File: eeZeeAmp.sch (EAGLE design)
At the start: 12 parts, among them IC1 LM386

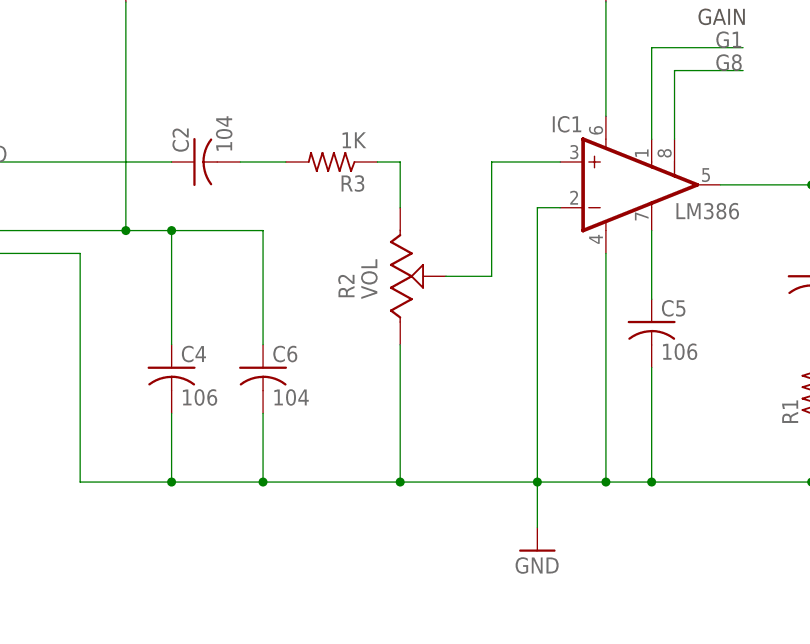
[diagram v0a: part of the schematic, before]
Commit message: Replaced offboard pot with pin header for clarity
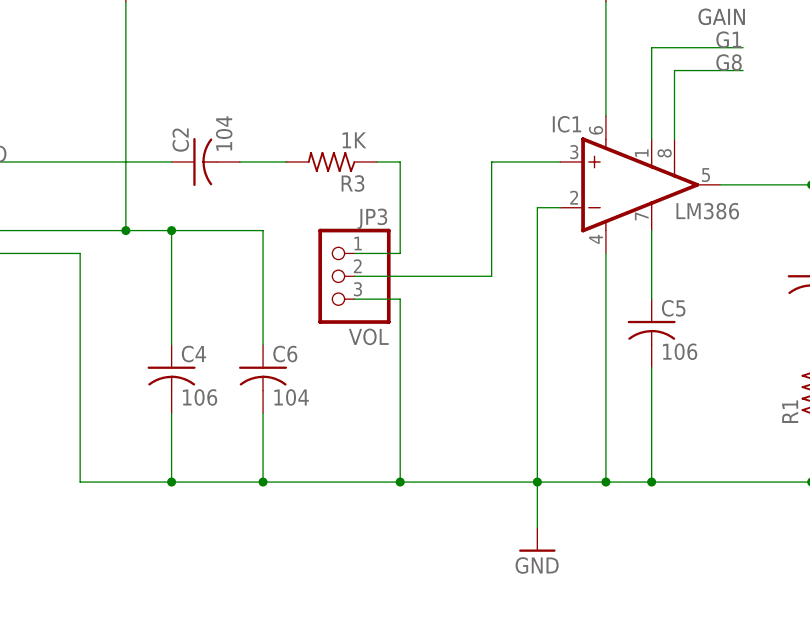
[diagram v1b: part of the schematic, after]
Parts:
- removed R2: VOL, bt:TRIM_US-
- added JP3: VOL, pinhead-2:PINHD-1X03_2.54-S
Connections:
- net GND: now also JP3.3; no longer R2.A
- net N$1: now also JP3.2; no longer R2.S
- net N$8: now also JP3.1; no longer R2.E
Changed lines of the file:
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@@
 <part name="C3" library="rcl" deviceset="C-US" device="C0603" value="503"/>
 <part name="R1" library="resistor" deviceset="R-US_" device="R0603" value="10"/>
-<part name="R2" library="bt" deviceset="TRIM_US-" device="" value="VOL"/>
 <part name="JP2" library="pinhead-2" deviceset="PINHD-1X02" device="_2.54-S" value="SPKR"/>
 <part name="R3" library="resistor" deviceset="R-US_" device="R0603" value="1K"/>
@@
 <part name="FRAME1" library="bt" deviceset="LETTER_L" device=""/>
 <part name="C6" library="rcl" deviceset="C-US" device="C0603" value="104"/>
+<part name="JP3" library="pinhead-2" deviceset="PINHD-1X03" device="_2.54-S" value="VOL"/>
 </parts>
 <sheets>
@@
 <instance part="C3" gate="G$1" x="154.94" y="101.6"/>
 <instance part="R1" gate="G$1" x="154.94" y="88.9" rot="R90"/>
-<instance part="R2" gate="1" x="109.22" y="101.6"/>
 <instance part="JP2" gate="A" x="185.42" y="109.22"/>
 <instance part="R3" gate="G$1" x="101.6" y="114.3" rot="R180"/>
@@
 <instance part="FRAME1" gate="G$2" x="147.32" y="2.54"/>
 <instance part="C6" gate="G$1" x="93.98" y="91.44"/>
+<instance part="JP3" gate="A" x="101.6" y="101.6" rot="MR0"/>
 </instances>
 <busses>
@@
 <segment>
 <pinref part="IC1" gate="G$1" pin="+IN"/>
-<pinref part="R2" gate="1" pin="S"/>
 <wire x1="127" y1="114.3" x2="119.38" y2="114.3" width="0.1524" layer="91"/>
 <wire x1="119.38" y1="114.3" x2="119.38" y2="101.6" width="0.1524" layer="91"/>
-<wire x1="119.38" y1="101.6" x2="114.3" y2="101.6" width="0.1524" layer="91"/>
+<pinref part="JP3" gate="A" pin="2"/>
+<wire x1="119.38" y1="101.6" x2="104.14" y2="101.6" width="0.1524" layer="91"/>
 </segment>
 </net>
@@
 <net name="N$8" class="0">
 <segment>
-<pinref part="R2" gate="1" pin="E"/>
 <pinref part="R3" gate="G$1" pin="1"/>
 <wire x1="106.68" y1="114.3" x2="109.22" y2="114.3" width="0.1524" layer="91"/>
-<wire x1="109.22" y1="114.3" x2="109.22" y2="109.22" width="0.1524" layer="91"/>
+<pinref part="JP3" gate="A" pin="1"/>
+<wire x1="104.14" y1="104.14" x2="109.22" y2="104.14" width="0.1524" layer="91"/>
+<wire x1="109.22" y1="104.14" x2="109.22" y2="114.3" width="0.1524" layer="91"/>
 </segment>
 </net>
@@
 <net name="GND" class="0">
 <segment>
-<pinref part="R2" gate="1" pin="A"/>
-<wire x1="109.22" y1="93.98" x2="109.22" y2="78.74" width="0.1524" layer="91"/>
+<wire x1="109.22" y1="99.06" x2="109.22" y2="78.74" width="0.1524" layer="91"/>
 <pinref part="R1" gate="G$1" pin="1"/>
 <wire x1="109.22" y1="78.74" x2="124.46" y2="78.74" width="0.1524" layer="91"/>
@@
 <wire x1="93.98" y1="86.36" x2="93.98" y2="78.74" width="0.1524" layer="91"/>
 <junction x="93.98" y="78.74"/>
+<pinref part="JP3" gate="A" pin="3"/>
+<wire x1="104.14" y1="99.06" x2="109.22" y2="99.06" width="0.1524" layer="91"/>
 </segment>
 </net>

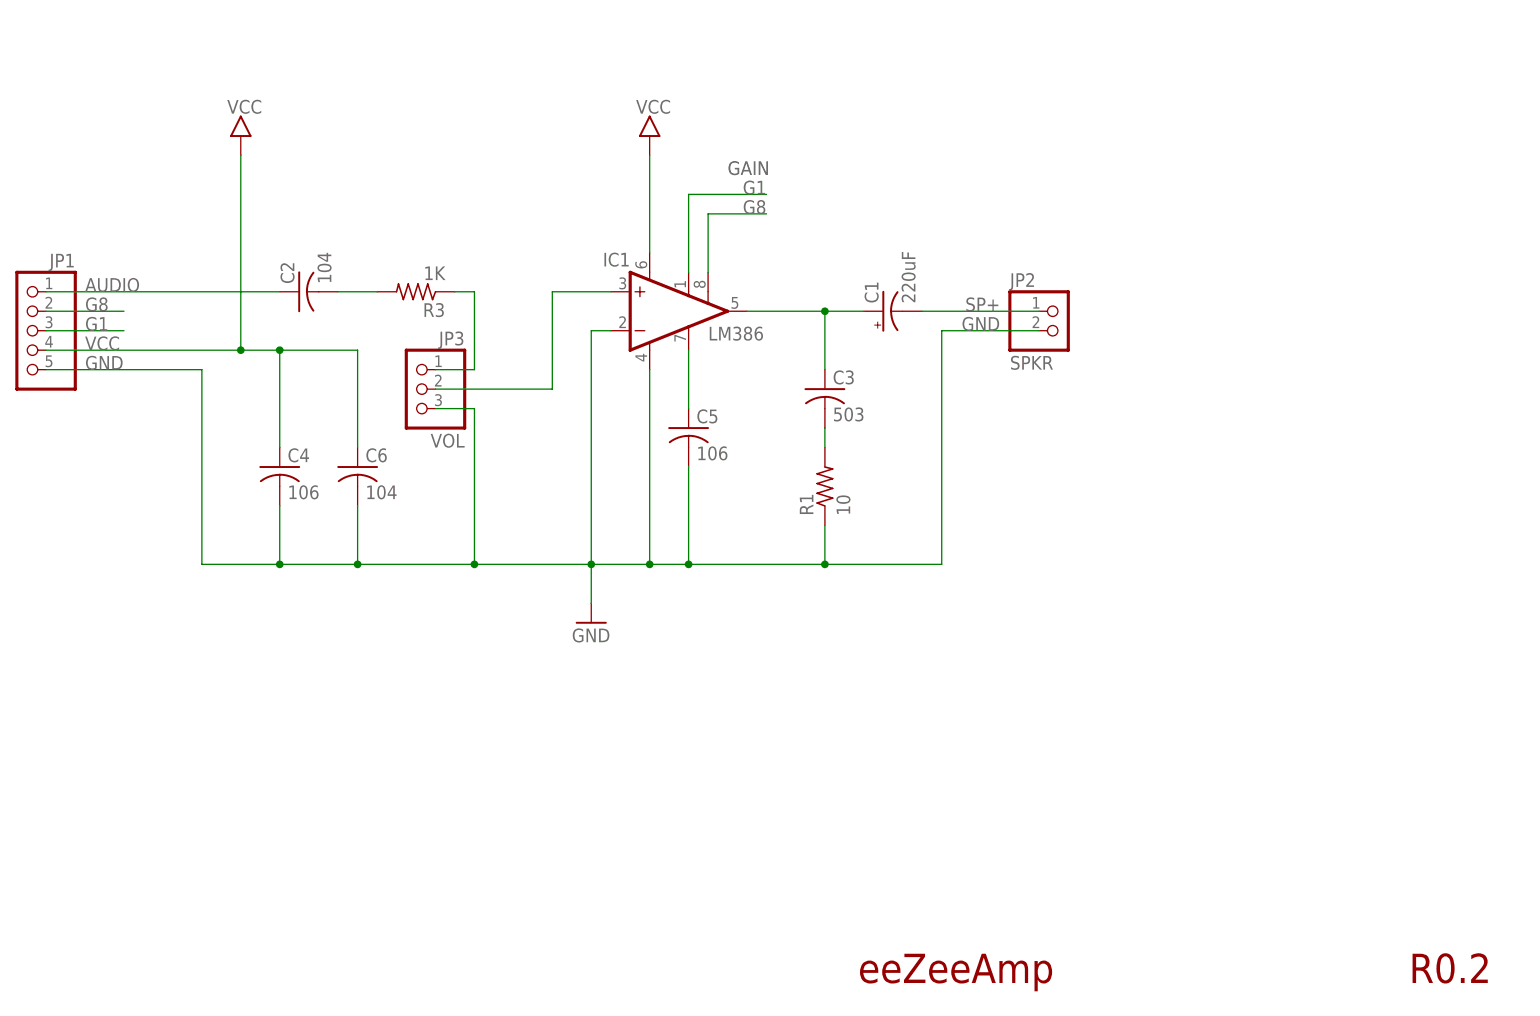
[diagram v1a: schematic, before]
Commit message: Revised pinout with single ground in attempt to remove ground loop. Revised schematic to use individual pin headers
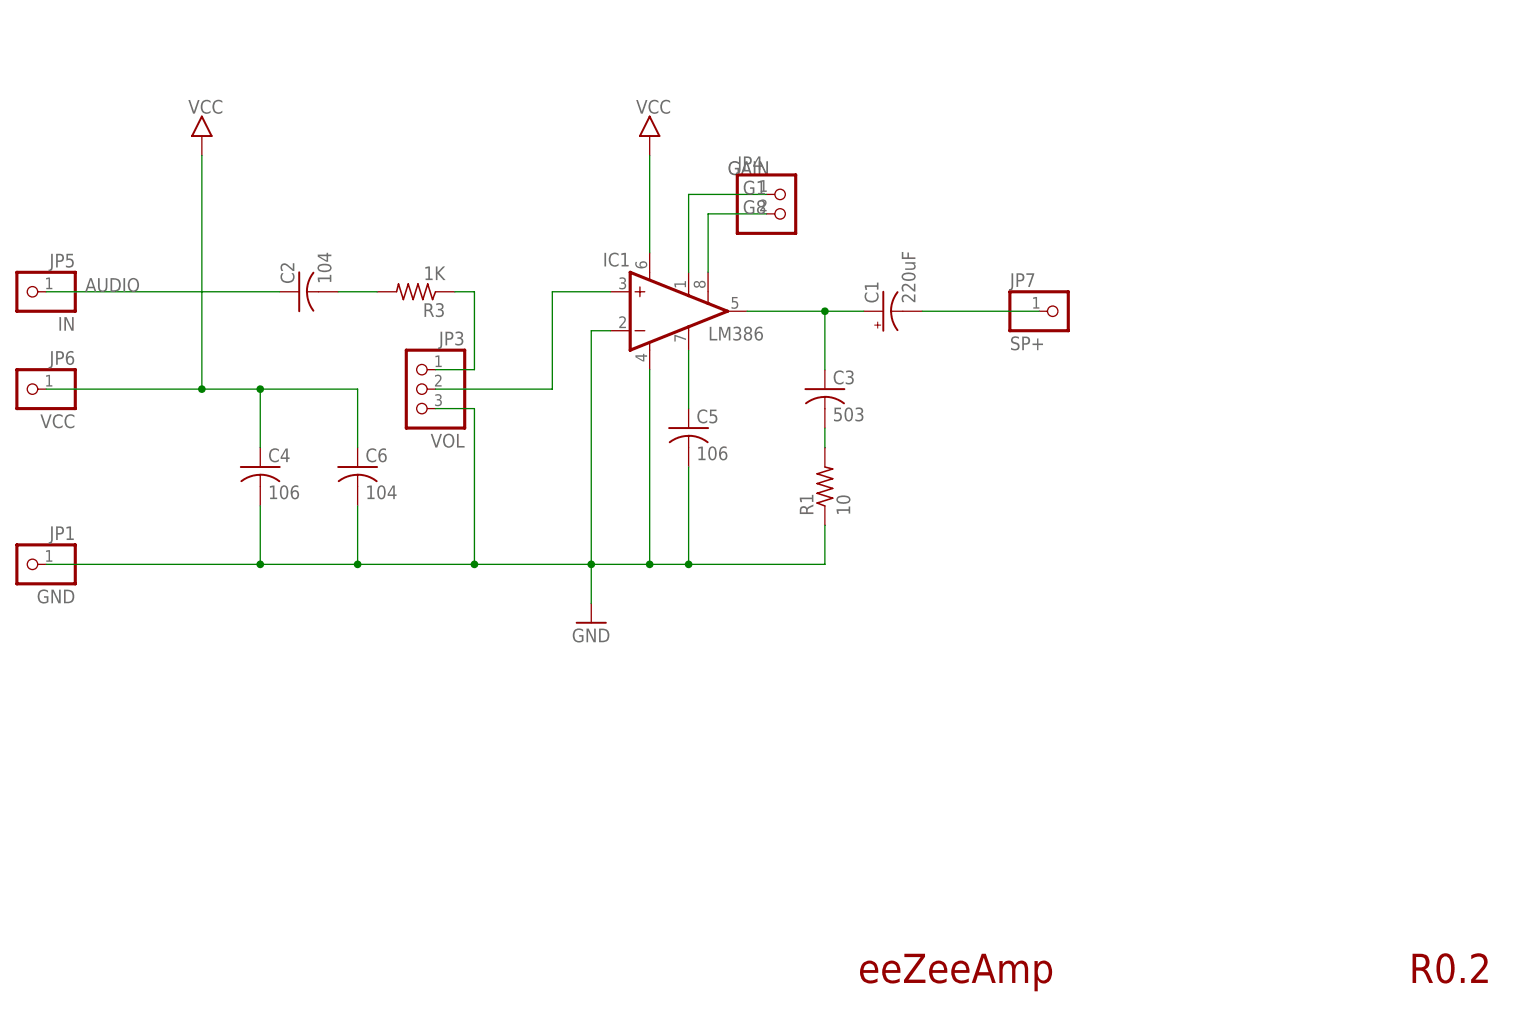
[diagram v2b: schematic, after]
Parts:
- removed JP2: SPKR, pinhead-2:PINHD-1X02_2.54-S
- added JP4: (no value), pinhead-2:PINHD-1X02_2.54-S
- added JP5: IN, pinhead-2:PINHD-1X01_2.54-S
- added JP6: VCC, pinhead-2:PINHD-1X01_2.54-S
- added JP7: SP+, pinhead-2:PINHD-1X01_2.54-S
- JP1: value (none) -> GND; device pinhead-2:PINHD-1X05_2.54-S -> pinhead-2:PINHD-1X01_2.54-S
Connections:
- net AUDIO: now also JP5.1; no longer JP1.1
- net G1: now also JP4.1; no longer JP1.3
- net G8: now also JP4.2; no longer JP1.2
- net GND: now also JP1.1; no longer JP1.5, JP2.2
- net SP+: now also JP7.1; no longer JP2.1
- net VCC: now also JP6.1; no longer JP1.4
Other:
- moved on the sheet: C4
